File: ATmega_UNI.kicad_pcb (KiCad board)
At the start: 2 copper layers, 53.3 x 68.6 mm, 47 parts, among them J1 PDIP_1_to_14, J11 PDIP_1_to_14, J13 3.3V, J2 PDIP_15_to_28, J22 PDIP_15_to_28, J5 PWR_Jack, J611 I2C, J612 I2C, J62 4uni, J63 4uni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

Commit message: mark doblesided parts
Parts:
- F1: footprint Fuse:Fuse_Bourns_MF-RHT100 -> Fuse:Fuse_Bourns_MF-R010
- J7: footprint Connector_PinSocket_2.54mm:PinSocket_1x06_P2.54mm_Horizontal -> Connector_PinSocket_2.54mm:PinSocket_1x06_P2.54mm_Horizontal_doublesided

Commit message: use power shield
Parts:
- removed C51, C52: 10uF, Capacitor_Tantalum_SMD:CP_EIA-3528-21_Kemet-B
- removed C54: 2.2uF, Capacitor_SMD:C_0805_2012Metric_Pad1.15x1.40mm_HandSolder
- removed C55: 0.01uF, Capacitor_SMD:C_0805_2012Metric_Pad1.15x1.40mm_HandSolder
- removed D5: D, Diode_SMD:D_SOD-323_HandSoldering_F_SilkS_Sym
- removed J5: PWR_Jack, Connector_BarrelJack:BarrelJack_Wuerth_6941xx301002
- removed U53: LP2985-3.3, Package_TO_SOT_SMD:SOT-23-5_no_lines
- removed U55: AMS1117-5.0, Package_TO_SOT_SMD:SOT-223-3_TabPin2
- added J95: Power, Connector_PinSocket_2.54mm:PinSocket_1x04_P2.54mm_Horizontal, F.Cu at (78.7, 53.3)
- added J98: extra_gnd, Connector_PinHeader_2.54mm:PinHeader_1x01_P2.54mm_Vertical_no_lines, F.Cu at (68.6, 66.0)
- added JP91: JCK→5V, Connector_PinHeader_2.54mm:PinHeader_1x02_P2.54mm_Vertical_no_lines, F.Cu at (86.4, 48.3)
- J79: footprint Connector_PinHeader_2.54mm:PinHeader_1x01_P2.54mm_Vertical -> Connector_PinHeader_2.54mm:PinHeader_1x01_P2.54mm_Vertical_no_lines
- JP9: value RAW→5V←TTL -> HDR→5V; footprint Connector_PinHeader_2.54mm:PinHeader_1x03_P2.54mm_Vertical_closed -> Connector_PinHeader_2.54mm:PinHeader_1x02_P2.54mm_Vertical_no_lines
- moved REF** 40.0 mm to (74.9, 64.8), turned to 0 degrees
- moved J7 3.59 mm to (111.8, 53.3)
- moved C2 2.54 mm to (92.2, 54.1)
- moved J79 2.54 mm to (114.3, 48.3)
- moved R2 2.27 mm to (92.2, 57.4)
- moved SW1 2.09 mm to (87.6, 55.6)
- moved R1 0.51 mm to (105.9, 59.7)
- moved R3 0.51 mm to (102.4, 59.7)
- turned JP9 to 0 degrees
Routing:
- net GND: track 439.8 -> 369.8 mm
- net +5V: track 114.2 -> 91.5 mm
- net RAW_JACK: track 11.6 -> 0.00 mm
- net Jack_5V: track 27.9 -> 17.5 mm
- net +3V3: track 113.4 -> 123.7 mm
- net RXD: track 116.5 -> 109.6 mm
- net TXD: track 121.3 -> 117.6 mm
- net USB_5V: track 37.6 -> 41.3 mm
- net DTR: track 10.2 -> 7.18 mm
- net Net-(C55-Pad2): track 1.99 -> 0.00 mm
- net ~RST: track 69.9 -> 71.9 mm
- net RAW: track 42.2 -> 44.0 mm
- net +5V_lim: track 114.7 -> 115.7 mm
- net SCL: track 143.6 -> 144.5 mm
- net SDA: track 149.7 -> 150.4 mm
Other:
- board text added: "5V←HDR"
- board text added: "5V←JCK"
- board text added: "HDR→5V"
- board text added: "JCK 5V"
- board text added: "JCK→5V"
- board text added: "RAW"
- board text removed: "3.3V/150mA"
- board text removed: "5V/800mA"
- board text removed: "HDR→5V←RAW"
- board text removed: "RAW<15V"
- board text removed: "RAW→5V←HDR"

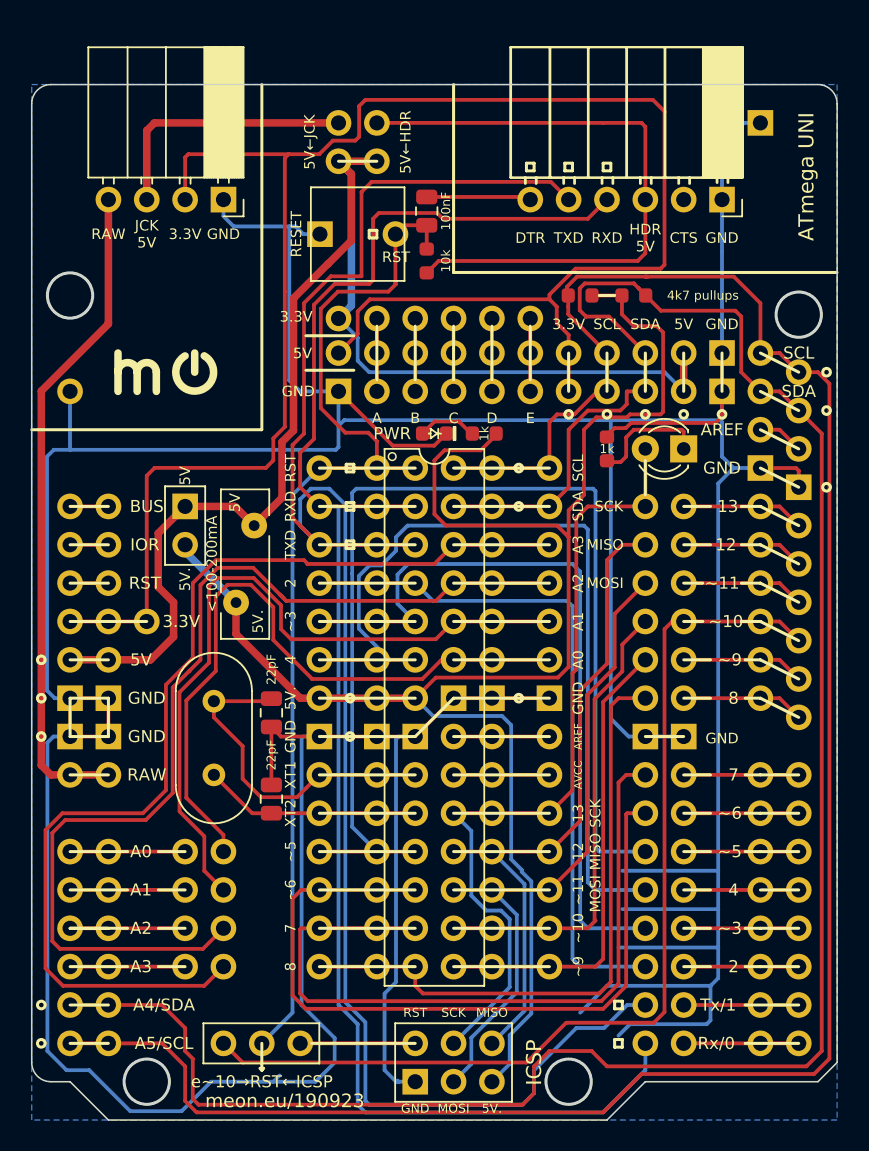
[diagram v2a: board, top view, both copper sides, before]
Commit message: add couple more universal pins
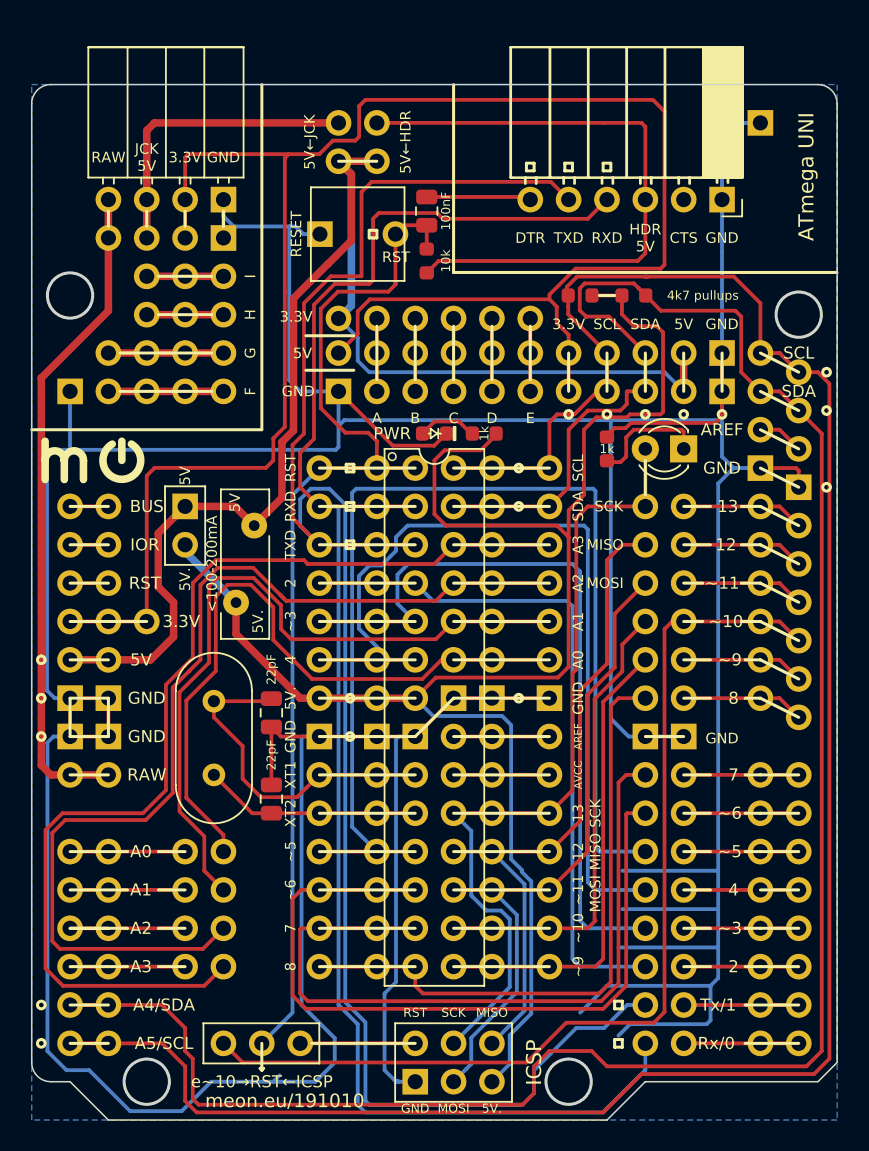
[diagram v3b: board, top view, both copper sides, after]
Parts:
- added J65: 4uni, Connector_PinHeader_2.54mm:PinHeader_1x04_P2.54mm_Vertical_no_lines, F.Cu at (78.7, 66.0)
- added J66: 4uni, Connector_PinHeader_2.54mm:PinHeader_1x04_P2.54mm_Vertical_no_lines, F.Cu at (76.2, 66.0)
- added J67: 4uni, Connector_PinHeader_2.54mm:PinHeader_1x04_P2.54mm_Vertical_no_lines, F.Cu at (73.7, 66.0)
- added J68: 2uni, Connector_PinHeader_2.54mm:PinHeader_1x02_P2.54mm_Vertical_no_lines, F.Cu at (71.1, 66.0)
- added J96: Power, Connector_PinHeader_2.54mm:PinHeader_1x04_P2.54mm_Vertical_no_lines, F.Cu at (78.7, 55.9)
- J95: footprint Connector_PinSocket_2.54mm:PinSocket_1x04_P2.54mm_Horizontal -> Connector_PinSocket_2.54mm:PinSocket_1x04_P2.54mm_Horizontal_doublesided
- moved REF** 7.58 mm to (70.1, 70.6)
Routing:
- net Net-(J65-Pad2): track 0.00 -> 7.62 mm
- net Net-(J65-Pad1): track 0.00 -> 7.62 mm
- net Net-(J65-Pad4): track 0.00 -> 5.08 mm
- net Net-(J65-Pad3): track 0.00 -> 5.08 mm
- net GND: track 369.8 -> 372.3 mm
- net +3V3: track 123.7 -> 126.2 mm
- net Jack_5V: track 17.5 -> 20.0 mm
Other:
- board text added: "F"
- board text added: "G"
- board text added: "H"
- board text added: "I"
- board text added: "meon.eu/191010"
- board text removed: "meon.eu/190923"

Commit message: all smd also as tht
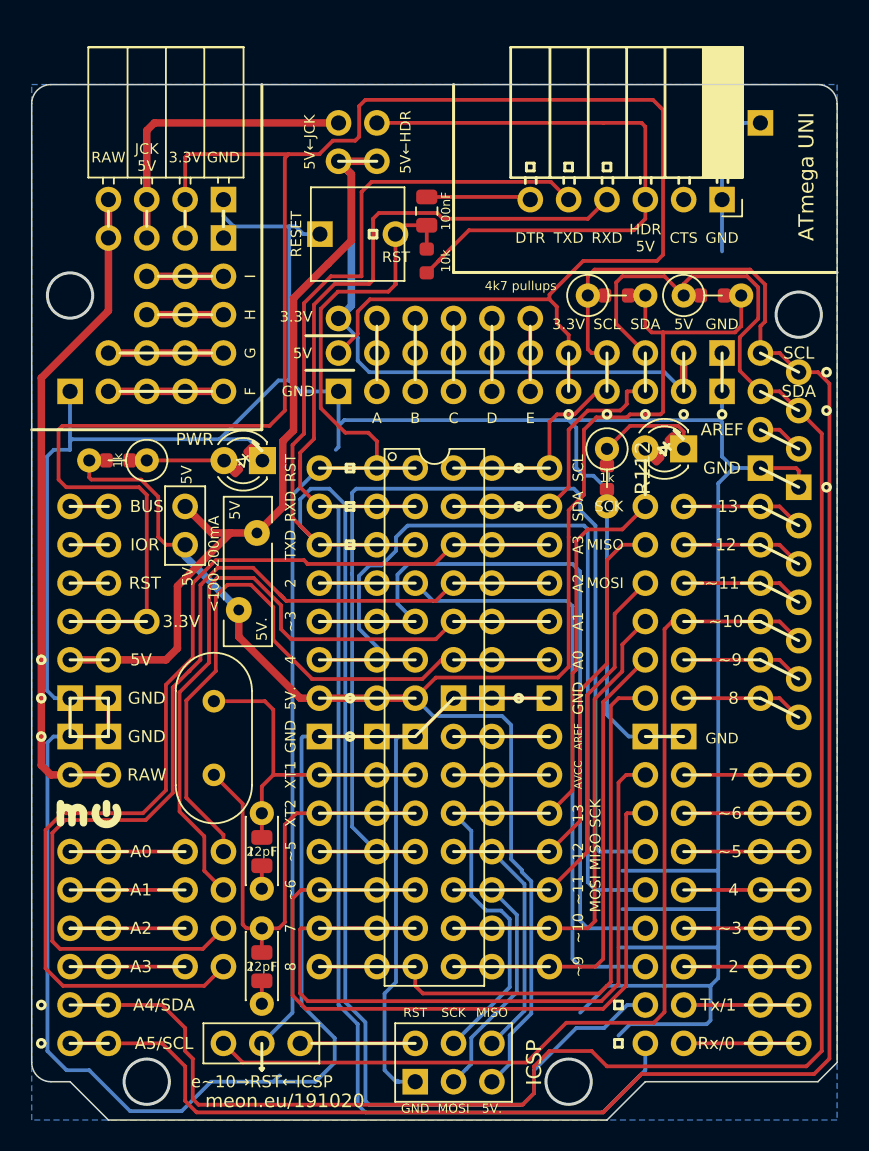
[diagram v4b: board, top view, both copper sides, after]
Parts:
- removed the REF** at (70.1, 70.6)
- added C13: 22pF, Capacitor_THT:C_Disc_D4.3mm_W1.9mm_P5.00mm, F.Cu at (81.3, 94.0)
- added C14: 22pF, Capacitor_THT:C_Disc_D4.3mm_W1.9mm_P5.00mm, F.Cu at (81.3, 101.6)
- added D12: PWR, LED_SMD.debian:LED_0603_1608Metric_symbol, F.Cu at (108.0, 69.8)
- added D92: PWR, LED_THT:LED_D3.0mm, F.Cu at (81.3, 70.6)
- added R112: 1k, Resistor_THT:R_Axial_DIN0207_L6.3mm_D2.5mm_P3.81mm_Vertical, F.Cu at (104.1, 69.8)
- added R12: 4k7 THT, Resistor_THT:R_Axial_DIN0207_L6.3mm_D2.5mm_P3.81mm_Vertical, F.Cu at (109.2, 59.7)
- added R32: 4k7 THT, Resistor_THT:R_Axial_DIN0207_L6.3mm_D2.5mm_P3.81mm_Vertical, F.Cu at (102.9, 59.7)
- added R92: 1k, Resistor_THT:R_Axial_DIN0207_L6.3mm_D2.5mm_P3.81mm_Vertical, F.Cu at (73.7, 70.6)
- added REF**: mo-logo-small, meon:mo-logo-small, F.Cu at (69.8, 94.0)
- moved R9 24.3 mm to (71.8, 70.6), turned to 180 degrees
- moved D9 12.8 mm to (80.1, 70.6), turned to 225 degrees
- moved C12 11.1 mm to (81.3, 104.1), turned to 270 degrees
- moved C11 9.21 mm to (81.3, 96.5)
- moved R1 5.21 mm to (111.1, 59.7), turned to 0 degrees
- moved R3 2.41 mm to (104.8, 59.7)
- moved R11 1.91 mm to (104.1, 71.8), turned to 270 degrees
- moved F1 0.52 mm to (81.0, 75.4)
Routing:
- net GND: track 372.3 -> 343.1 mm
- net XTAL2: track 14.4 -> 30.8 mm
- net +3V3: track 126.2 -> 137.1 mm
- net Net-(D9-Pad2): track 3.88 -> 6.71 mm
- net SCL: track 144.5 -> 146.5 mm
- net SDA: track 150.4 -> 152.1 mm
- net USB_5V: track 41.3 -> 40.0 mm
- net Net-(D1-Pad1): track 7.91 -> 9.08 mm
- net PDIP11: track 74.1 -> 73.4 mm
- net +5V_lim: track 115.7 -> 116.4 mm
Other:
- board text added: "meon.eu/191020"
- board text removed: "meon.eu/191010"

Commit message: add i2c top connector, dtr+r-reset also tht
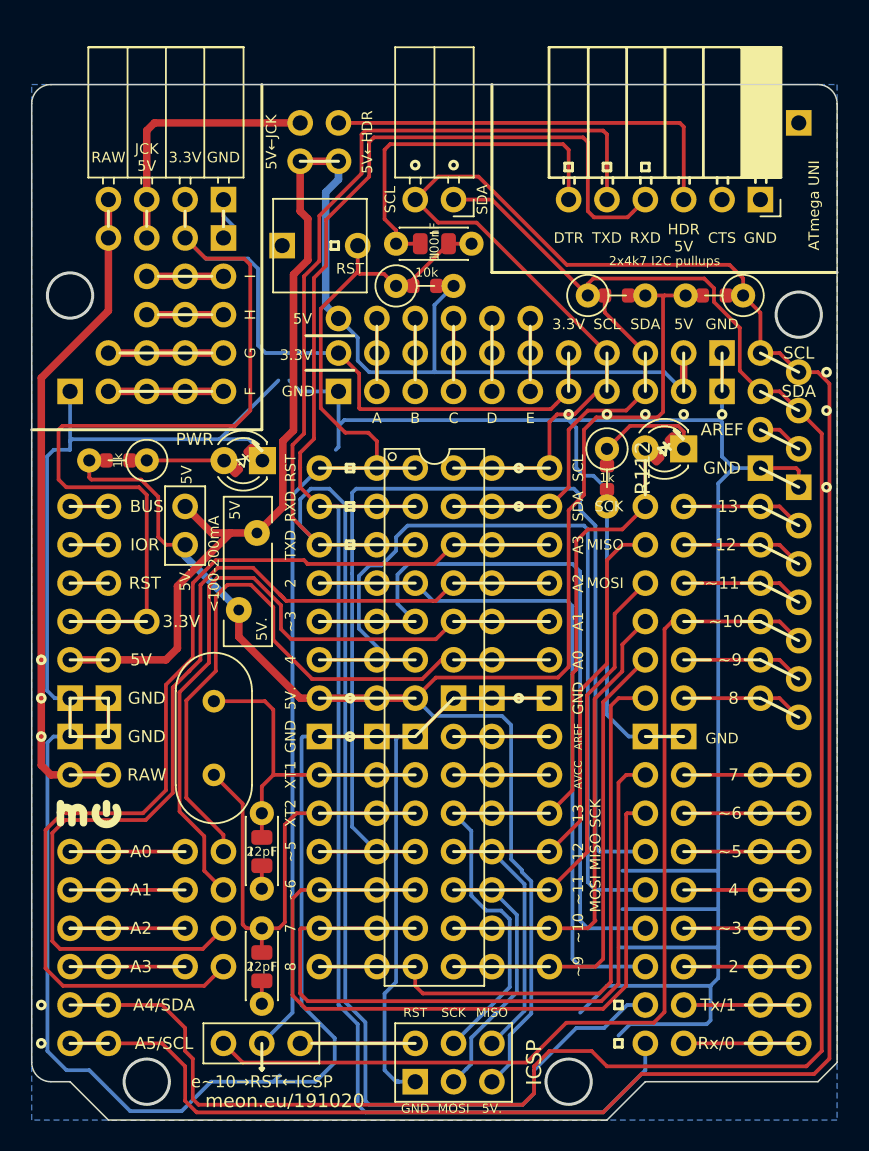
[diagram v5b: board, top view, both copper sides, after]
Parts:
- added C22: 100nF, Capacitor_THT:C_Disc_D4.3mm_W1.9mm_P5.00mm, F.Cu at (90.2, 56.3)
- added J613: I2C, Connector_PinSocket_2.54mm:PinSocket_1x02_P2.54mm_Horizontal_doubleside, F.Cu at (94.0, 53.3)
- added R22: 10k THT, Resistor_THT:R_Axial_DIN0207_L6.3mm_D2.5mm_P3.81mm_Vertical, F.Cu at (90.2, 59.1)
- R3: value 4k7 pullups -> 2x4k7 I2C pullups
- moved R32 10.3 mm to (113.2, 59.7), turned to 180 degrees
- moved R3 6.48 mm to (111.3, 59.7), turned to 180 degrees
- moved R1 6.35 mm to (104.8, 59.7)
- moved R12 6.35 mm to (102.9, 59.7)
- moved SW1 2.61 mm to (85.1, 56.4)
- moved J79 2.54 mm to (116.8, 48.3)
- moved JP9 2.54 mm to (86.4, 48.3)
- moved JP91 2.54 mm to (83.8, 48.3)
- moved J7 2.54 mm to (114.3, 53.3)
- moved C2 2.22 mm to (92.7, 56.3), turned to 180 degrees
- moved R2 1.66 mm to (92.1, 59.1), turned to 180 degrees
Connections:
- R2 pad 1: USB_5V -> +5V
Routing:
- net +3V3: track 137.1 -> 90.9 mm
- net GND: track 343.1 -> 316.1 mm
- net SCL: track 146.5 -> 170.3 mm
- net DTR: track 7.18 -> 24.2 mm
- net USB_5V: track 40.0 -> 27.8 mm
- net RXD: track 109.6 -> 120.7 mm
- net TXD: track 117.6 -> 126.5 mm
- net SDA: track 152.1 -> 160.9 mm
- net +5V: track 91.5 -> 97.5 mm
- net +5V_lim: track 116.4 -> 110.8 mm
- net Jack_5V: track 20.0 -> 17.5 mm
- net ~RST: track 71.9 -> 73.8 mm
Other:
- board text removed: "RESET"

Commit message: clean-up
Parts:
- moved R22 5.08 mm to (95.2, 58.9), turned to 180 degrees
- moved R2 1.27 mm to (93.3, 58.9), turned to 0 degrees
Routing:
- net GND: track 316.1 -> 402.4 mm
- net TXD: track 126.5 -> 118.0 mm
- net ~RST: track 73.8 -> 77.6 mm
- net RXD: track 120.7 -> 122.0 mm
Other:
- board text added: "2x4k7 I2C pullups"

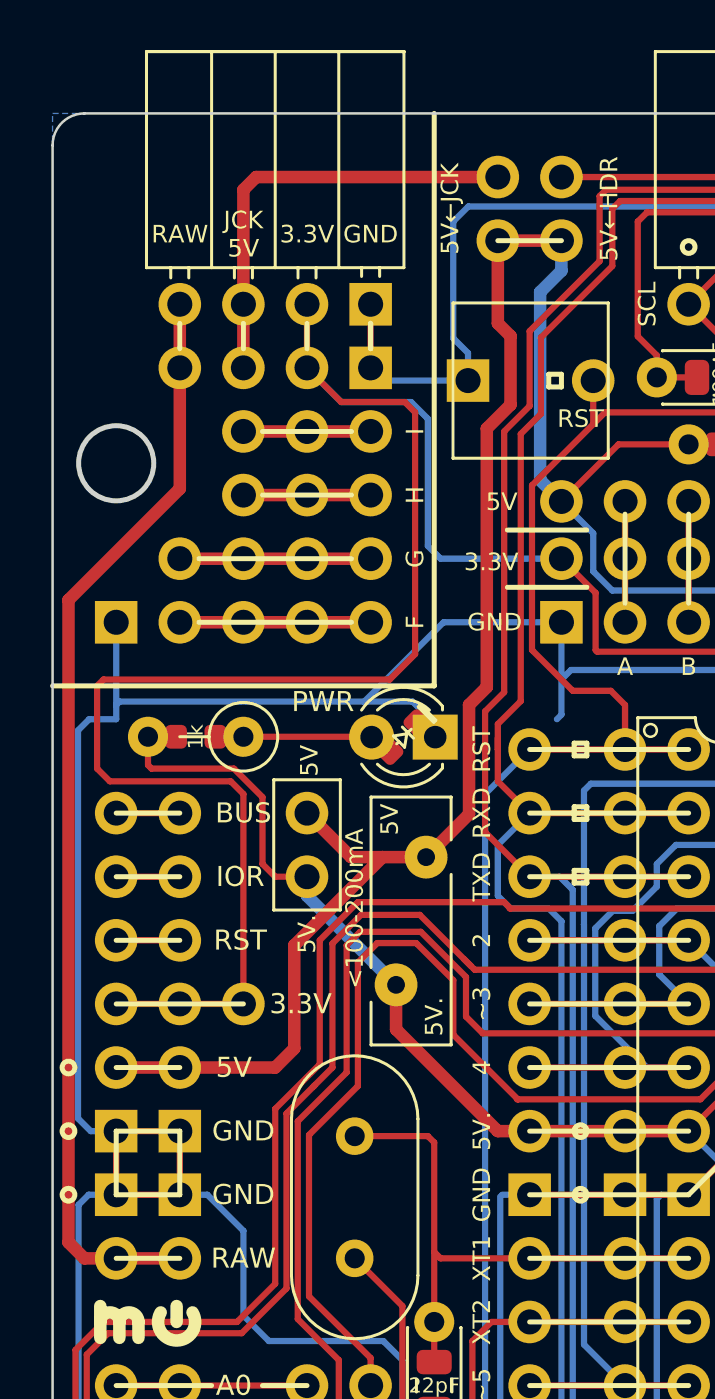
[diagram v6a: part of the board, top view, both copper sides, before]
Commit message: add jack connector
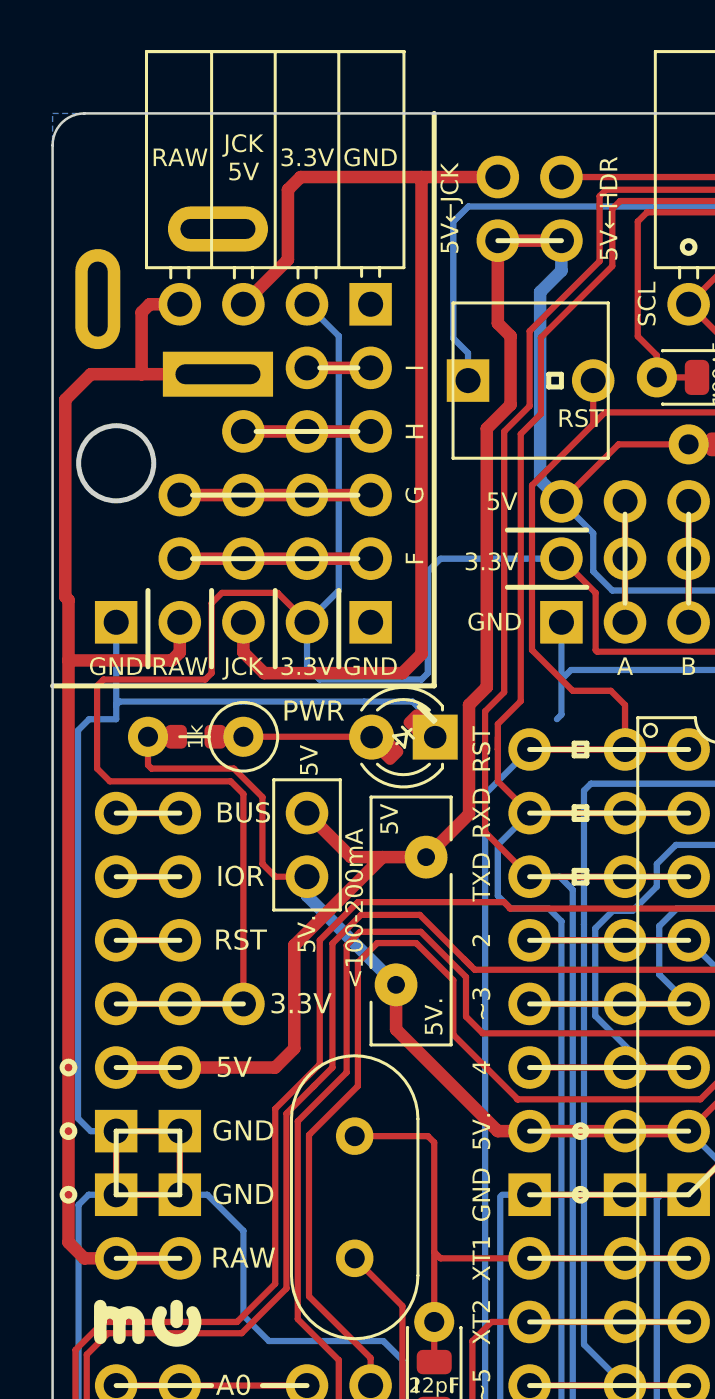
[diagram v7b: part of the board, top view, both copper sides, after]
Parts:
- added J97: Barrel_Jack_Switch, Connector_BarrelJack:BarrelJack_Wuerth_6941xx301002_no_lines, F.Cu at (72.6, 56.1)
- J67: footprint Connector_PinHeader_2.54mm:PinHeader_1x04_P2.54mm_Vertical_no_lines -> Connector_PinHeader_2.54mm:PinHeader_1x03_P2.54mm_Vertical_no_lines
- R3: value 2x4k7 I2C pullups -> 4k7 pullups
- moved J96 10.2 mm to (78.7, 66.0)
- moved J65 2.54 mm to (78.7, 63.5)
- moved J66 2.54 mm to (76.2, 63.5)
- moved J67 2.54 mm to (73.7, 63.5)
- moved J68 2.54 mm to (71.1, 63.5)
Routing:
- net Jack_5V: track 17.5 -> 41.9 mm
- net GND: track 402.4 -> 386.6 mm
- net RAW: track 44.0 -> 54.8 mm
- net +3V3: track 90.9 -> 86.5 mm
- net Net-(J65-Pad4): track 5.08 -> 2.54 mm
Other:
- board text added: "JCK"

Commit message: tidy-up
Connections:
- R1 pad 2: +5V_lim -> +5V
- R12 pad 2: +5V_lim -> +5V
- R3 pad 2: +5V_lim -> +5V
- R32 pad 2: +5V_lim -> +5V
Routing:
- net +5V_lim: track 110.8 -> 65.3 mm
- net +5V: track 97.3 -> 106.1 mm
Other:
- board text added: "2x~RST"
- board text added: "~RST"
